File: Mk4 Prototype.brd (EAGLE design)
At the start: 121.6 x 80 mm, 269 parts, among them IC1 MSP432E401, IC10 TPD3E001DRL, IC11 LMV358ID, IC12 SN74HC4066D, IC13 TPA2006D1, IC14 TPD4S012, IC15 CC3120R, IC2 AS4C4M16SA-7TCN, IC3 MX25R1635FM1IL0, IC4 TCA9555, IC5 SIM800C, IC6 SST26VF016B-104I/SM, IC7 TPD3E001DRL, IC8 BQ25601, IC9 TPS62082, J1 78723-1001, J2 ER-CON50HT-1, J3 2x5 1.27mm, J4 GSM-COIL-ANT, J5 S2B-PH-SM4-TB(LF)(SN), Q1 2N7002PW, Q2 2N7002PW, Q3 CSD25402Q3A, Q8 CSD13202Q2, SW1 JOYSTICK, U1 ZX62-B-5PA(33), U4 MIC-4MM, U5 LDMS1540S-01-R8-0.8-R, X1 ABS07-32.768KHZ-T, X2 ABM8G-25.000MHZ-B4Y-T, X3 ABS07-32.768KHZ-T, X4 ABM8G-40.000MHZ-4Y-T3

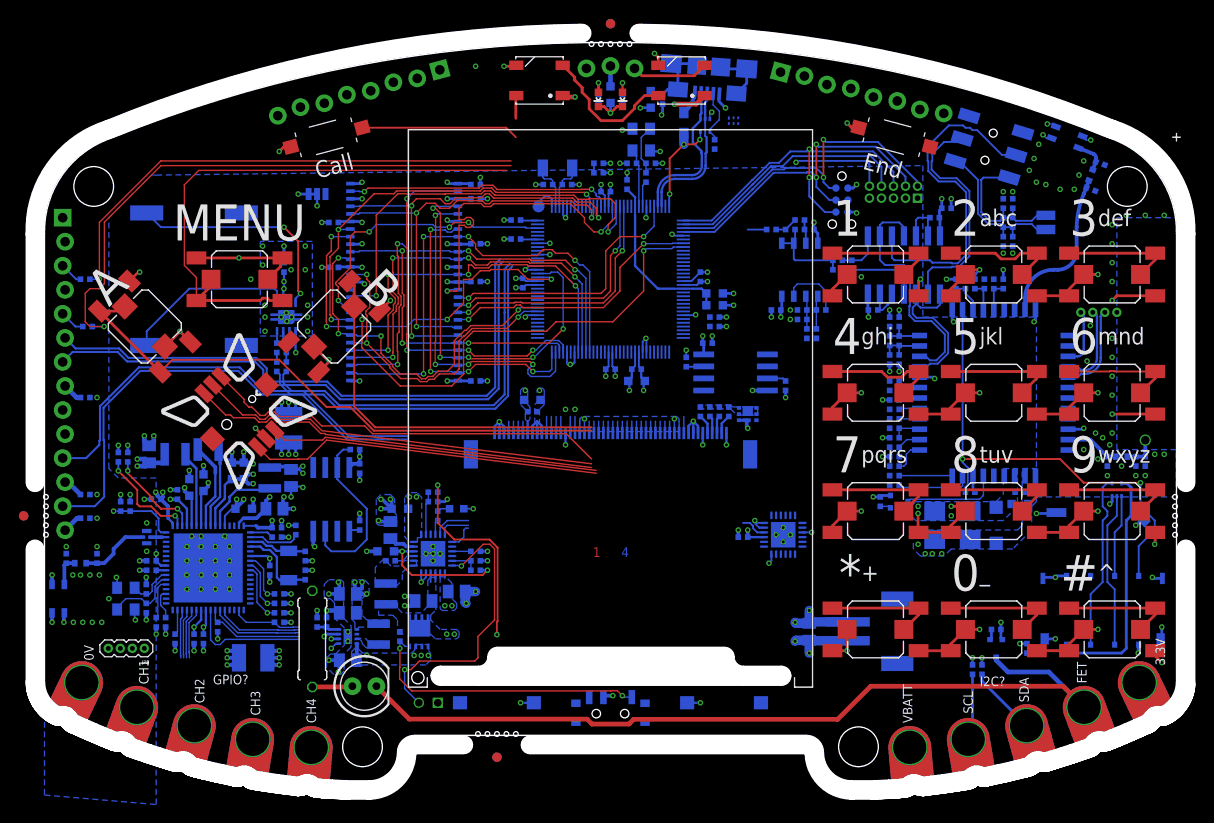
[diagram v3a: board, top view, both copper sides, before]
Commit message: Added tmp102, swapped out TPS62, more routing
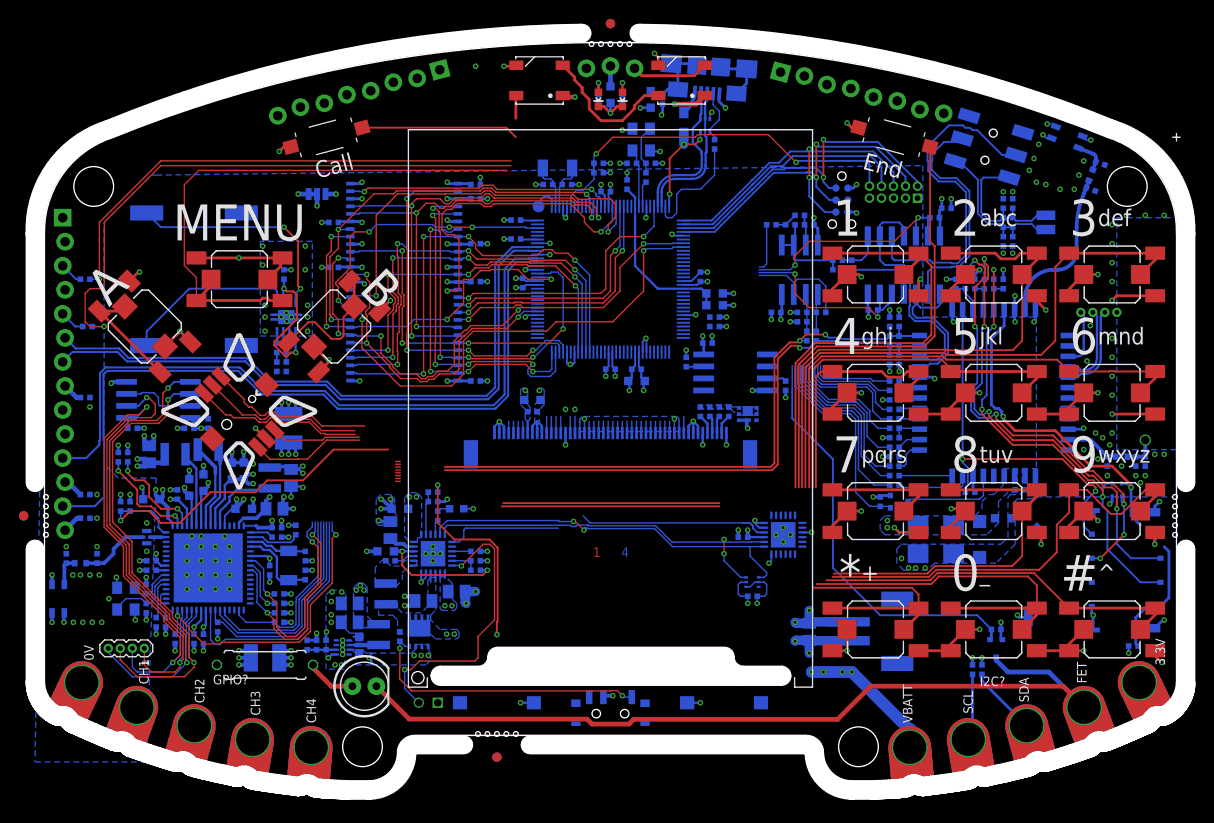
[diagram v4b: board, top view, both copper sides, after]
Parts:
- removed IC9: TPS62082, TiLDA Mk4 Parts:WSON8
- added C102: 0402/100n/10V/X5R, TiLDA Mk4 Parts:C0402-SMALLER
- added C103: 0402/120p/50V/C0G, TiLDA Mk4 Parts:C0402-SMALLER
- added U2: TMP102, TiLDA Mk4 Parts:SOT563
- C46: value 0805/10u/10V/X5R -> 0603/4u7/10V/X5R; device TiLDA Mk4 Parts:C0805-N -> TiLDA Mk4 Parts:C0603K-SMALL
- C86: value 0402/1u/10V/X5R -> 0603/1u/6V3/X5R; device TiLDA Mk4 Parts:C0402-SMALLER -> TiLDA Mk4 Parts:C0603K-SMALL
- IC11: device TiLDA Mk4 Parts:SO08-SPARK-NEW -> TiLDA Mk4 Parts:SO08
- IC14: value TPD4S012 -> MX25R1635FM1IL0; device TiLDA Mk4 Parts:SON-6 -> TiLDA Mk4 Parts:SO08-EIAJ
- IC3: value MX25R1635FM1IL0 -> TPS62882; device TiLDA Mk4 Parts:SO08-EIAJ -> TiLDA Mk4 Parts:VSON-HR
- IC4: value TCA9555 -> TCA9555RGER
- R60, R61: value (none) -> 0402/??
- X4: value ABM8G-40.000MHZ-4Y-T3 -> ABM8-40.000MHZ-10-1-U-T
- moved IC14 67.5 mm to (-47.8, 40.2), turned to 90 degrees
- moved R67 26.1 mm to (-50.5, 37.2), turned to 180 degrees
- moved C59 18.5 mm to (-44.5, 37.2), turned to 180 degrees
- moved R66 15.7 mm to (-42.5, 37.8), turned to 90 degrees
- moved IC3 15.7 mm to (-28.3, 14.1), turned to 180 degrees
- moved C51 11.3 mm to (55.2, 14.2), turned to 180 degrees
- moved J1 9.10 mm to (57.5, 22.2), turned to 180 degrees
- moved R11 5.71 mm to (-36.5, 12.2), turned to 180 degrees
- moved R60 2.40 mm to (-31.1, 14.3)
- moved R61 2.40 mm to (-30.1, 14.3)
- moved C29 2.30 mm to (36.2, 25.5)
- moved C30 2.30 mm to (41.5, 27.8)
- moved C32 2.30 mm to (32.5, 25.5)
- moved D1 2.30 mm to (39.0, 25.5)
- moved C46 2.00 mm to (-26.6, 14.3), turned to 90 degrees
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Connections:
- removed net VCC: IC14.4
- net 3V3: now also C102.1, C103.1, IC14.8, U2.5; no longer IC3.8, IC9.5
- net FLASH_!CS: now also IC14.1; no longer IC3.1
- net FLASH_CLK: now also IC14.6; no longer IC3.6
- net FLASH_MISO: now also IC14.2; no longer IC3.2
- net FLASH_MOSI: now also IC14.5; no longer IC3.5
- net FLASH_PU: now also IC14.3, IC14.7; no longer IC3.3, IC3.7
- net GND: now also C102.2, IC14.4, IC3.3, IC3.5, U2.2, U2.4; no longer IC14.6, IC3.4, IC9.2, IC9.3, IC9.EP
- net I2C5_SCL: now also U2.1
- net I2C5_SDA: now also U2.6
- net SW: now also IC3.6; no longer IC9.7
- net TPS_FB: now also C103.2, IC3.2; no longer IC9.4
- net VBATT: now also IC3.1, IC3.7; no longer IC9.1, IC9.8
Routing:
- net BTN_3: track 12.0 -> 62.2 mm
- net FLASH_MOSI: track 5.30 -> 55.5 mm, vias 0 -> 2
- net FLASH_CLK: track 5.38 -> 54.8 mm, vias 0 -> 2
- net BTN_END: track 0.00 -> 48.8 mm
- net FLASH_MISO: track 5.22 -> 50.4 mm, vias 0 -> 2
- net BTN_2: track 12.5 -> 56.7 mm
- net FLASH_!CS: track 6.28 -> 49.8 mm, vias 0 -> 2
- net SPK_N: track 22.3 -> 65.6 mm, vias 0 -> 2
- net SPK_P: track 21.9 -> 64.8 mm, vias 0 -> 1
- net FET: track 1.14 -> 43.8 mm
- net BTN_6: track 12.0 -> 53.2 mm
- net SIM_DATA: track 8.73 -> 49.8 mm, vias 0 -> 6
- net BTN_1: track 12.0 -> 49.9 mm
- net I2C5_SDA: track 3.30 -> 41.0 mm, vias 0 -> 2
- net I2C5_SCL: track 4.01 -> 41.2 mm, vias 0 -> 2
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- removed copper zone on layer 16, net SW

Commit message: Day 5? routing done for prototype
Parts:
- removed JP5, JP6: 1x08, TiLDA Mk4 Parts:1X08_LOCK
- added C104: 0402/100n/10V/X5R, TiLDA Mk4 Parts:C0402-SMALLER
- added IC9: OPT3001, TiLDA Mk4 Parts:USON-6
- added LOGO1: EMFLOGO-BOTH, TiLDA Mk4 Parts:EMFLOGO
- added TP2, TP3, TP4, TP5, TP6, TP7: TP, TiLDA Mk4 Parts:B1,27
- C88, C89, C90: value 0603/4u7/10V/X5R -> 0402/4u7/6V3/X5R; device TiLDA Mk4 Parts:C0603K-SMALL -> TiLDA Mk4 Parts:C0402-SMALLER
- IC3: value TPS62882 -> TPS62822DLCR
- L4: value SRN2512-2R2M -> DFE201610E-R47M=P2; device TiLDA Mk4 Parts:1008 -> TiLDA Mk4 Parts:0806
- R60: value 0402/?? -> 0402/732K/5%
- R61: value 0402/?? -> 0402/162K/5%
- moved R21 25.0 mm to (-13.9, 48.2), turned to 90 degrees
- moved R22 24.0 mm to (-12.9, 48.2), turned to 90 degrees
- moved L8 1.50 mm to (-42.5, 33.5), turned to 270 degrees
- moved L7 1.39 mm to (-45.5, 33.2)
- moved C90 1.30 mm to (-43.1, 30.2)
- moved C88 1.00 mm to (-44.4, 30.0)
- moved C63 0.72 mm to (-48.1, 34.1)
- moved C14 0.50 mm to (2.75, 41.8)
- moved C2 0.50 mm to (9.75, 46.2)
- moved IC6 0.50 mm to (12.7, 43.1)
- moved R10 0.50 mm to (18.0, 41.8)
- moved R9 0.50 mm to (7.50, 44.2)
- moved L4 0.30 mm to (-24.5, 15.2)
- moved C89 0.25 mm to (-38.8, 28.5)
- moved C15 0.25 mm to (-1.50, 64.2)
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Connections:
- removed net AIN5_PD6: IC1.127
- removed net CH1: PCB.CH4
- removed net CH2: PCB.CH3
- removed net CH3: PCB.CH2
- removed net I2C2_SCL: PCB.SCL, R24.1
- removed net I2C2_SDA: PCB.SDA, R23.1
- removed net I2C5_SCL: IC1.121, IC4.19, IC8.5, R22.1, U2.1
- removed net I2C5_SDA: IC1.120, IC4.20, IC8.6, R21.1, U2.6
- removed net MCP_INT: IC1.33, IC4.22
- removed net PB2: IC1.91
- removed net PL5: IC1.86
- removed net PN3: IC1.110
- removed net PN4: IC1.111
- removed net PN5: IC1.112
- removed net SIM_RI: R32.1
- removed net SIM_RX: IC1.117
- removed net SIM_RXD: R37.1
- removed net SIM_TX: IC1.116
- removed net SIM_TXD: R36.1
- removed net UART2_RX: IC1.125, IC15.55, R68.1
- removed net UART2_TX: IC1.126, IC15.57, R69.1
- removed net WS2812: IC1.123, LED1.4
- new net AIN5_CH3: IC1.127, PCB.CH2
- new net I2C5_EXT_SCL: IC1.121, PCB.SCL, R24.1
- new net I2C5_EXT_SDA: IC1.120, PCB.SDA, R23.1
- new net I2C9_SCL: IC1.33, IC4.19, IC8.5, IC9.4, R22.1, U2.1
- new net I2C9_SDA: IC1.34, IC4.20, IC8.6, IC9.6, R21.1, U2.6
- new net T3CCPO_WS2812: IC1.125, LED1.4
- new net TCA_INT: IC1.15, IC4.22
- new net UART1_SIM_RI: IC1.112, R32.1
- new net UART1_SIM_RX: IC1.95, R36.1
- new net UART1_SIM_TX: IC1.96, R37.1
- new net UART3_CC_RX: IC1.116, IC15.55, R68.1
- new net UART3_CC_TX: IC1.117, IC15.57, R69.1
- new net UART5_EXT_RX: IC1.18, PCB.CH3
- new net UART5_EXT_TX: IC1.19, PCB.CH4
- net 3V3: now also C104.1, IC9.1
- net BQ_!INT: now also IC1.14; no longer IC1.124
- net BTN_10: now also IC4.14; no longer IC4.11
- net BTN_11: now also IC4.13; no longer IC4.12
- net BTN_12: now also IC4.12; no longer IC4.13
- net BTN_2: now also IC4.3; no longer IC4.2
- net BTN_3: now also IC4.4; no longer IC4.3
- net BTN_4: now also IC4.7; no longer IC4.4
- net BTN_5: now also IC4.6; no longer IC4.5
- net BTN_6: now also IC4.5; no longer IC4.6
- net BTN_7: now also IC4.8; no longer IC4.7
- net BTN_8: now also IC4.10; no longer IC4.8
- net BTN_9: now also IC4.11; no longer IC4.10
- net BTN_CALL: now also IC4.15; no longer IC4.14
- net BTN_END: now also IC4.2; no longer IC4.15
- net BTN_MENU: now also IC1.60; no longer IC1.34
- net CC_!HIB: now also IC1.124; no longer IC1.14
- net CC_!RESET: now also IC1.118; no longer IC1.18
- net CC_IRQ: now also IC1.123; no longer IC1.15
- net CH4: now also IC1.126
- net FET: now also IC1.110; no longer IC1.85
- net GND: now also C104.2, IC9.2, IC9.3, IC9.PAD; no longer JP5.1, JP6.1
- net JOY_CEN: now also IC1.72; no longer IC1.118
- net JOY_DOWN: now also IC1.74; no longer IC1.107
- net JOY_RIGHT: now also IC1.91; no longer IC1.74
- net LCD_!RST: now also IC1.111; no longer IC1.21
- net LCD_TEAR: now also IC1.21; no longer IC1.19
- net LED1: now also IC1.86; no longer IC1.43
- net LED2: now also IC1.85; no longer IC1.44
- net MUX_A: now also IC1.105; no longer IC1.108
- net MUX_B: now also IC1.106; no longer IC1.109
- net SIM_CTS: now also TP4.TP
- net SIM_DCD: now also TP3.TP
- net SIM_DTR: now also TP2.TP
- net SIM_NETLIGHT: now also IC1.108; no longer IC1.105
- net SIM_PWR_KEY: now also IC1.109; no longer IC1.106
- net SIM_RTS: now also TP5.TP
- net SIM_STATUS: now also IC1.107; no longer IC1.102
- net T_X: now also IC1.43; no longer IC1.60
- net T_Y: now also IC1.44; no longer IC1.72
- net USB_ID: now also TP6.TP; no longer IC1.95
- net VBUS: now also TP7.TP; no longer IC1.96
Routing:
- net !WAKE: track 1.82 -> 157.5 mm, vias 0 -> 4
- net BTN_CALL: track 16.7 -> 137.8 mm, vias 0 -> 3
- net I2C9_SDA: track 0.00 -> 93.2 mm, vias 0 -> 9
- net I2C9_SCL: track 0.00 -> 90.0 mm, vias 0 -> 8
- net UART3_CC_RX: track 0.00 -> 84.3 mm, vias 0 -> 2
- net !RESET: track 40.5 -> 122.7 mm, vias 2 -> 5
- net UART5_EXT_TX: track 0.00 -> 82.1 mm, vias 0 -> 3
- net AIN5_CH3: track 0.00 -> 81.4 mm, vias 0 -> 1
- net UART3_CC_TX: track 0.00 -> 81.3 mm, vias 0 -> 2
- net UART5_EXT_RX: track 0.00 -> 78.4 mm, vias 0 -> 3
- net CH4: track 0.00 -> 78.1 mm, vias 0 -> 1
- net I2C5_EXT_SDA: track 0.00 -> 68.2 mm
- net I2C5_EXT_SCL: track 0.00 -> 64.0 mm
- net BTN_A: track 35.0 -> 93.2 mm, vias 0 -> 3
- net CC_!RESET: track 39.7 -> 96.9 mm, vias 1 -> 2
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- added copper zone on layer 1, net 3V3
- added copper zone on layer 1, net GND
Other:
- board text added: "GPIO"
- board text added: "I2C5"
- board text removed: "GND"
- board text removed: "GPIO?"
- board text removed: "I2C?"

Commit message: Gerber tweaks
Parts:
- moved C39 0.05 mm to (-23.8, 24.2)
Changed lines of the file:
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@@
 <setting verticaltext="up"/>
 </settings>
-<grid distance="0.5" unitdist="mm" unit="mm" style="lines" multiple="1" display="yes" altdistance="0.25" altunitdist="mm" altunit="mm"/>
+<grid distance="0.1" unitdist="mm" unit="mm" style="lines" multiple="1" display="yes" altdistance="0.05" altunitdist="mm" altunit="mm"/>
 <layers>
 <layer number="1" name="Top" color="4" fill="1" visible="yes" active="yes"/>
-<layer number="2" name="3V3@2" color="1" fill="3" visible="no" active="yes"/>
+<layer number="2" name="3V3@2" color="1" fill="3" visible="yes" active="yes"/>
 <layer number="3" name="Route3" color="4" fill="3" visible="no" active="no"/>
 <layer number="4" name="Route4" color="1" fill="4" visible="no" active="no"/>
@@
 <layer number="13" name="Route13" color="4" fill="5" visible="no" active="no"/>
 <layer number="14" name="Route14" color="1" fill="6" visible="no" active="no"/>
-<layer number="15" name="GND@3" color="4" fill="6" visible="no" active="yes"/>
+<layer number="15" name="GND@3" color="4" fill="6" visible="yes" active="yes"/>
 <layer number="16" name="Bottom" color="1" fill="1" visible="yes" active="yes"/>
 <layer number="17" name="Pads" color="2" fill="1" visible="yes" active="yes"/>
@@
 <element name="R16" library="TiLDA Mk4 Parts" package="R0402-SMALLER" value="0402/10K/5%" x="-14.25" y="22.25" rot="MR180"/>
 <element name="C36" library="TiLDA Mk4 Parts" package="C0805-N" value="0805/10u/10V/X5R" x="-23.25" y="26.5" rot="MR90"/>
-<element name="C39" library="TiLDA Mk4 Parts" package="C0603K-SMALL" value="0603/4u7/10V/X5R" x="-23.75" y="24.25" rot="MR180"/>
+<element name="C39" library="TiLDA Mk4 Parts" package="C0603K-SMALL" value="0603/4u7/10V/X5R" x="-23.8" y="24.25" rot="MR180"/>
 <element name="C37" library="TiLDA Mk4 Parts" package="C0402-SMALLER" value="0402/47n/10V/X5R" x="-23.25" y="23.25" rot="MR0"/>
 <element name="L1" library="TiLDA Mk4 Parts" package="1008" value="SRN2512-2R2M" x="-23.75" y="19.75" rot="MR270"/>
@@
 <vertex x="28" y="0" curve="30.8"/>
 <vertex x="59.8" y="9"/>
+<vertex x="59.8" y="35"/>
+<vertex x="53.5" y="35"/>
+<vertex x="53.5" y="60"/>
 <vertex x="59.8" y="60" curve="64.112019"/>
 <vertex x="53.25" y="67.75" curve="24.117056"/>
@@
 <polygon width="0.15" layer="16" isolate="0.254" rank="6">
 <vertex x="-59.8" y="60"/>
-<vertex x="-59.8" y="8.5"/>
-<vertex x="-49" y="4"/>
+<vertex x="-59.8" y="16"/>
+<vertex x="-49" y="11"/>
 <vertex x="-48" y="32"/>
 <vertex x="-52" y="32"/>
@@
 <vertex x="59.8" y="35"/>
 <vertex x="53.5" y="35"/>
-<vertex x="53.5" y="59.5"/>
-<vertex x="59.8" y="59.5"/>
+<vertex x="53.5" y="60"/>
 <vertex x="59.8" y="60" curve="64.112019"/>
 <vertex x="53.25" y="67.75" curve="24.117056"/>
@@
 <via x="53" y="56.75" extent="1-16" drill="0.3"/>
 <via x="53" y="58.75" extent="1-16" drill="0.3"/>
-<via x="54.5" y="59.75" extent="1-16" drill="0.3"/>
-<via x="56.5" y="59.75" extent="1-16" drill="0.3"/>
-<via x="58.5" y="59.75" extent="1-16" drill="0.3"/>
+<via x="53" y="60.35" extent="1-16" drill="0.3"/>
+<via x="56.4" y="60.35" extent="1-16" drill="0.3"/>
+<via x="58.4" y="60.35" extent="1-16" drill="0.3"/>
 <wire x1="57.55" y1="51.25" x2="53.5" y2="51.25" width="0.3" layer="1"/>
 <wire x1="53.5" y1="51.25" x2="53" y2="50.75" width="0.3" layer="1"/>
@@
 <wire x1="-23.25" y1="27.4" x2="-24.4" y2="27.4" width="0.4" layer="16"/>
 <wire x1="-24.4" y1="27.4" x2="-24.5" y2="27.5" width="0.4" layer="16"/>
-<wire x1="-25.75" y1="24.25" x2="-24.625" y2="24.25" width="0.4" layer="16"/>
+<wire x1="-25.75" y1="24.25" x2="-24.675" y2="24.25" width="0.4" layer="16"/>
 <wire x1="-13.75" y1="23.25" x2="-13" y2="23.25" width="0.3" layer="16"/>
 <wire x1="-13.75" y1="24.25" x2="-13" y2="24.25" width="0.3" layer="16"/>
@@
 <polygon width="0.15" layer="1" rank="6">
 <vertex x="-59.8" y="39"/>
-<vertex x="-59.8" y="8.5" curve="33.907324"/>
-<vertex x="-23" y="0"/>
-<vertex x="-22.5" y="0"/>
+<vertex x="-59.8" y="16" curve="33.907324"/>
+<vertex x="-23" y="7.5"/>
+<vertex x="-22.5" y="7.5"/>
 <vertex x="-22.5" y="39"/>
 </polygon>
@@
 <vertex x="28" y="0" curve="30.8"/>
 <vertex x="59.8" y="9"/>
+<vertex x="59.8" y="35"/>
+<vertex x="53.5" y="35"/>
+<vertex x="53.5" y="60"/>
 <vertex x="59.8" y="60" curve="64.112019"/>
 <vertex x="53.25" y="67.75" curve="24.117056"/>
@@
 <via x="-22" y="24.25" extent="1-16" drill="0.3"/>
 <via x="-13" y="22.25" extent="1-16" drill="0.3"/>
-<wire x1="-22.875" y1="24.25" x2="-22" y2="24.25" width="0.4" layer="16"/>
+<wire x1="-22.925" y1="24.25" x2="-22" y2="24.25" width="0.4" layer="16"/>
 <wire x1="-20.775" y1="24.25" x2="-22" y2="24.25" width="0.25" layer="16"/>
 <wire x1="-13.75" y1="22.25" x2="-13" y2="22.25" width="0.3" layer="16"/>
@@
 <wire x1="29.575" y1="28.85" x2="29.425" y2="29" width="0.15" layer="16"/>
 <wire x1="29.425" y1="29" x2="28.5" y2="29" width="0.15" layer="16"/>
-<wire x1="28.5" y1="29" x2="25.4" y2="29" width="0.15" layer="16"/>
-<wire x1="25.4" y1="29" x2="23.9" y2="30.5" width="0.15" layer="16"/>
+<wire x1="28.5" y1="29" x2="27.4" y2="29" width="0.15" layer="16"/>
+<wire x1="27.4" y1="29" x2="27" y2="29.4" width="0.15" layer="16"/>
+<wire x1="27" y1="29.4" x2="25" y2="29.4" width="0.15" layer="16"/>
+<wire x1="25" y1="29.4" x2="24.7" y2="29.7" width="0.15" layer="16"/>
+<wire x1="24.7" y1="29.7" x2="23.9" y2="30.5" width="0.15" layer="16"/>
 <wire x1="23.9" y1="38.2" x2="23.3" y2="38.8" width="0.15" layer="16"/>
 <wire x1="23.9" y1="30.5" x2="23.9" y2="38.2" width="0.15" layer="16"/>
@@
 <wire x1="-43" y1="15.5" x2="-43" y2="16.25" width="0.25" layer="16"/>
 <wire x1="-43" y1="16.25" x2="-43" y2="17" width="1" layer="2"/>
-<wire x1="-41.25" y1="18.75" x2="-36.25" y2="18.75" width="1" layer="2"/>
-<wire x1="-43" y1="17" x2="-41.25" y2="18.75" width="1" layer="2"/>
+<wire x1="-37.25" y1="18.75" x2="-36.25" y2="18.75" width="1" layer="2"/>
+<wire x1="-43" y1="17" x2="-42.5" y2="17.5" width="1" layer="2"/>
+<wire x1="-42.5" y1="17.5" x2="-38.5" y2="17.5" width="1" layer="2"/>
+<wire x1="-38.5" y1="17.5" x2="-37.25" y2="18.75" width="1" layer="2"/>
 <wire x1="-36.25" y1="18.75" x2="-35.75" y2="18.75" width="1" layer="2"/>
 <wire x1="-35.75" y1="18.75" x2="-34.7" y2="19.8" width="1" layer="2"/>
